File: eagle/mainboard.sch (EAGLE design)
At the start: 73 parts, among them IC1 74HC02D, IC2 74HC151D, IC3 74HC151D, IC4 74HC590D

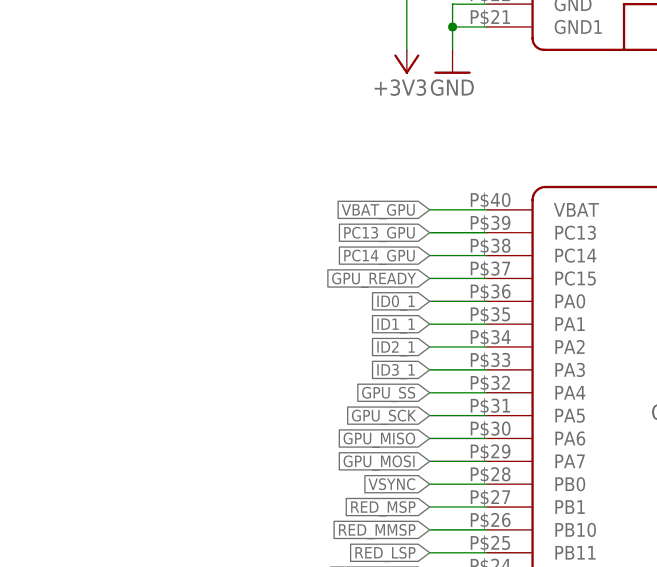
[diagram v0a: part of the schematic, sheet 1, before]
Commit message: pcb: gpu ready led
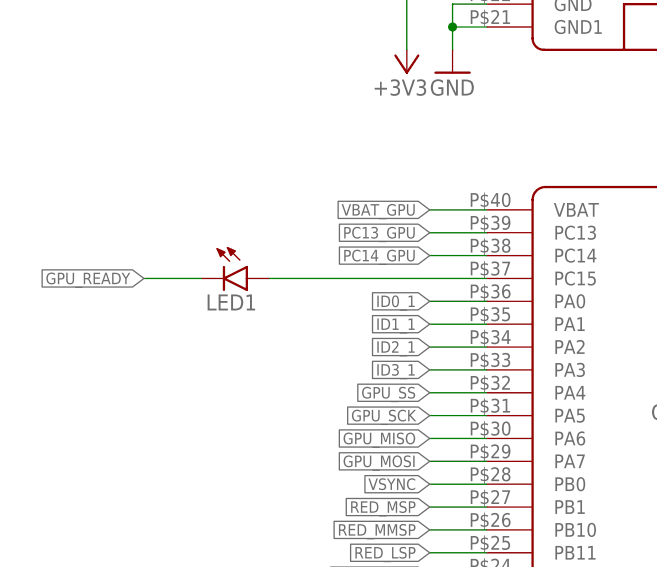
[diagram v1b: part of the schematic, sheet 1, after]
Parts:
- added LED1: (no value), led:LEDCHIPLED_0805
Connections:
- new net N$1: GPU.PC15, LED1.A
- net GPU_READY: now also LED1.C; no longer GPU.PC15
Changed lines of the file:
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@@
 <setting verticaltext="up"/>
 </settings>
-<grid distance="0.1" unitdist="inch" unit="inch" style="lines" multiple="1" display="no" altdistance="0.01" altunitdist="inch" altunit="inch"/>
+<grid distance="50" unitdist="mil" unit="mil" style="dots" multiple="1" display="yes" altdistance="0.01" altunitdist="inch" altunit="inch"/>
 <layers>
 <layer number="1" name="Top" color="4" fill="1" visible="no" active="no"/>
@@
 <part name="GND19" library="supply1" library_urn="urn:adsk.eagle:library:371" deviceset="GND" device=""/>
 <part name="GND22" library="supply1" library_urn="urn:adsk.eagle:library:371" deviceset="GND" device=""/>
+<part name="LED1" library="led" library_urn="urn:adsk.eagle:library:259" deviceset="LED" device="CHIPLED_0805" package3d_urn="urn:adsk.eagle:package:15821/2"/>
 </parts>
 <sheets>
@@
 <attribute name="VALUE" x="350.52" y="33.02" size="1.778" layer="96"/>
 </instance>
+<instance part="LED1" gate="G$1" x="77.47" y="92.71" smashed="yes" rot="R270">
+<attribute name="NAME" x="72.898" y="89.154" size="1.778" layer="95"/>
+<attribute name="VALUE" x="72.898" y="86.995" size="1.778" layer="96"/>
+</instance>
 </instances>
 <busses>
@@
 <net name="GPU_READY" class="0">
 <segment>
-<wire x1="97.79" y1="92.71" x2="104.14" y2="92.71" width="0.1524" layer="91"/>
-<label x="97.79" y="92.71" size="1.27" layer="95" rot="R180" xref="yes"/>
-<pinref part="GPU" gate="G$1" pin="PC15"/>
-</segment>
-<segment>
 <wire x1="97.79" y1="161.29" x2="104.14" y2="161.29" width="0.1524" layer="91"/>
 <label x="97.79" y="161.29" size="1.27" layer="95" rot="R180" xref="yes"/>
 <pinref part="CPU" gate="G$1" pin="PC15"/>
+</segment>
+<segment>
+<wire x1="66.04" y1="92.71" x2="72.39" y2="92.71" width="0.1524" layer="91"/>
+<label x="66.04" y="92.71" size="1.27" layer="95" rot="R180" xref="yes"/>
+<pinref part="LED1" gate="G$1" pin="C"/>
 </segment>
 </net>
@@
 </segment>
 </net>
+<net name="N$1" class="0">
+<segment>
+<pinref part="LED1" gate="G$1" pin="A"/>
+<pinref part="GPU" gate="G$1" pin="PC15"/>
+<wire x1="80.01" y1="92.71" x2="104.14" y2="92.71" width="0.1524" layer="91"/>
+</segment>
+</net>

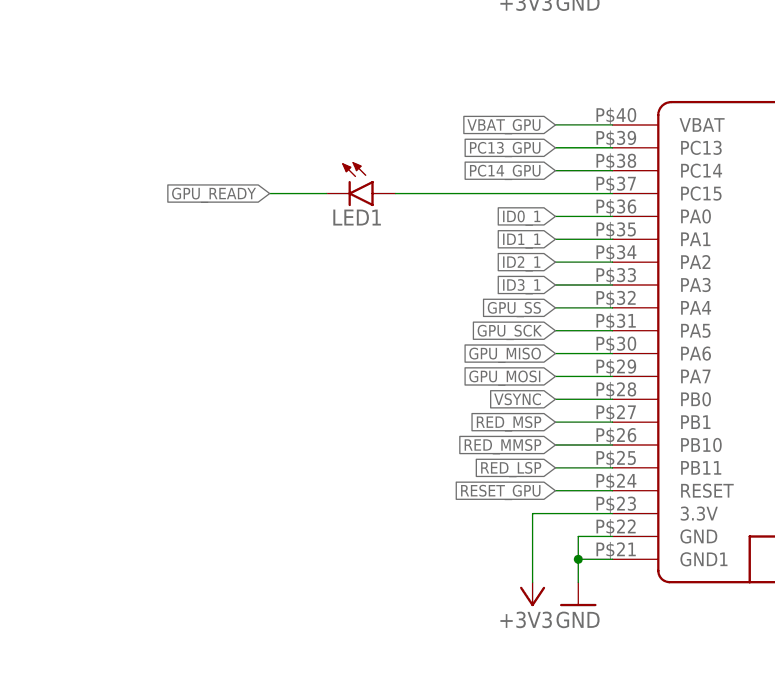
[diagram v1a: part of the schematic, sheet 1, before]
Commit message: made D-pad quadrtatic, corrected other minor stuff
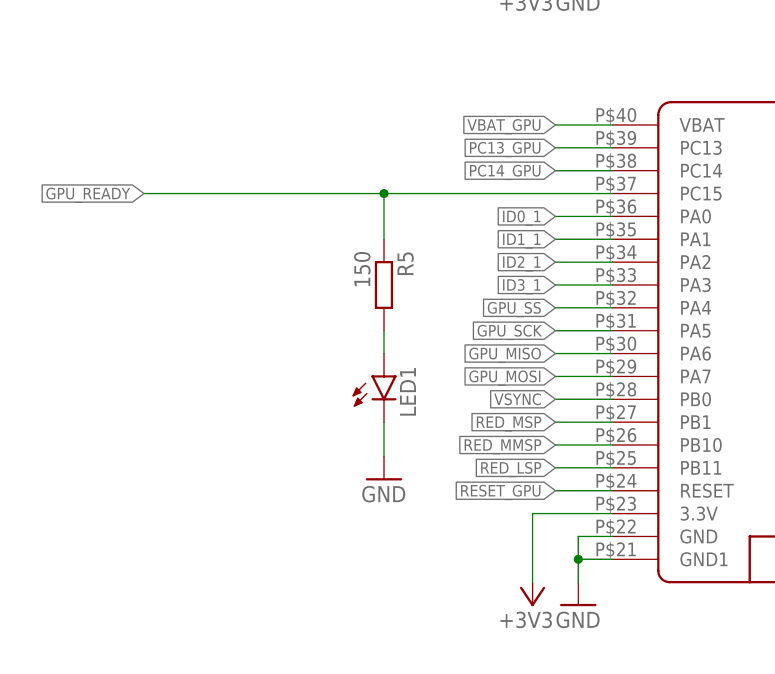
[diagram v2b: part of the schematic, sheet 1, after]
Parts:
- added R5: 150, rcl:R-EU_R0805
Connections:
- net GND: now also LED1.C
- net GPU_READY: now also GPU.PC15, R5.1; no longer LED1.C
- net N$1: now also R5.2; no longer GPU.PC15
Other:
- moved on the sheet: LED1
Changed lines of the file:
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@@
 <setting verticaltext="up"/>
 </settings>
-<grid distance="50" unitdist="mil" unit="mil" style="dots" multiple="1" display="yes" altdistance="0.01" altunitdist="inch" altunit="inch"/>
+<grid distance="0.1" unitdist="inch" unit="inch" style="lines" multiple="1" display="no" altdistance="0.01" altunitdist="inch" altunit="inch"/>
 <layers>
 <layer number="1" name="Top" color="4" fill="1" visible="no" active="no"/>
@@
 <part name="GND22" library="supply1" library_urn="urn:adsk.eagle:library:371" deviceset="GND" device=""/>
 <part name="LED1" library="led" library_urn="urn:adsk.eagle:library:259" deviceset="LED" device="CHIPLED_0805" package3d_urn="urn:adsk.eagle:package:15821/2"/>
+<part name="R5" library="rcl" library_urn="urn:adsk.eagle:library:334" deviceset="R-EU_" device="R0805" package3d_urn="urn:adsk.eagle:package:23553/2" value="150"/>
+<part name="GND32" library="supply1" library_urn="urn:adsk.eagle:library:371" deviceset="GND" device=""/>
 </parts>
 <sheets>
@@
 <attribute name="VALUE" x="350.52" y="33.02" size="1.778" layer="96"/>
 </instance>
-<instance part="LED1" gate="G$1" x="77.47" y="92.71" smashed="yes" rot="R270">
-<attribute name="NAME" x="72.898" y="89.154" size="1.778" layer="95"/>
-<attribute name="VALUE" x="72.898" y="86.995" size="1.778" layer="96"/>
+<instance part="LED1" gate="G$1" x="78.74" y="72.39" smashed="yes">
+<attribute name="NAME" x="82.296" y="67.818" size="1.778" layer="95" rot="R90"/>
+<attribute name="VALUE" x="84.455" y="67.818" size="1.778" layer="96" rot="R90"/>
+</instance>
+<instance part="R5" gate="G$1" x="78.74" y="82.55" smashed="yes" rot="R270">
+<attribute name="NAME" x="80.2386" y="86.36" size="1.778" layer="95" rot="R270"/>
+<attribute name="VALUE" x="75.438" y="86.36" size="1.778" layer="96" rot="R270"/>
+</instance>
+<instance part="GND32" gate="1" x="78.74" y="60.96" smashed="yes">
+<attribute name="VALUE" x="76.2" y="58.42" size="1.778" layer="96"/>
 </instance>
 </instances>
@@
 <pinref part="GND13" gate="1" pin="GND"/>
 </segment>
+<segment>
+<pinref part="LED1" gate="G$1" pin="C"/>
+<wire x1="78.74" y1="67.31" x2="78.74" y2="63.5" width="0.1524" layer="91"/>
+<pinref part="GND32" gate="1" pin="GND"/>
+</segment>
 </net>
 <net name="GPU_MOSI" class="0">
@@
 </segment>
 <segment>
-<wire x1="66.04" y1="92.71" x2="72.39" y2="92.71" width="0.1524" layer="91"/>
-<label x="66.04" y="92.71" size="1.27" layer="95" rot="R180" xref="yes"/>
-<pinref part="LED1" gate="G$1" pin="C"/>
+<label x="52.07" y="92.71" size="1.27" layer="95" rot="R180" xref="yes"/>
+<pinref part="R5" gate="G$1" pin="1"/>
+<wire x1="78.74" y1="92.71" x2="52.07" y2="92.71" width="0.1524" layer="91"/>
+<wire x1="78.74" y1="87.63" x2="78.74" y2="92.71" width="0.1524" layer="91"/>
+<pinref part="GPU" gate="G$1" pin="PC15"/>
+<wire x1="104.14" y1="92.71" x2="78.74" y2="92.71" width="0.1524" layer="91"/>
+<junction x="78.74" y="92.71"/>
 </segment>
 </net>
@@
 <net name="N$1" class="0">
 <segment>
+<pinref part="R5" gate="G$1" pin="2"/>
 <pinref part="LED1" gate="G$1" pin="A"/>
-<pinref part="GPU" gate="G$1" pin="PC15"/>
-<wire x1="80.01" y1="92.71" x2="104.14" y2="92.71" width="0.1524" layer="91"/>
-</segment>
-</net>
+<wire x1="78.74" y1="74.93" x2="78.74" y2="77.47" width="0.1524" layer="91"/>
+</segment>
+</net>

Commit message: added svg art and finished todo list
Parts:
- added JP5: (no value), pinhead:PINHD-1X2
- added LED2: (no value), led:LEDCHIPLED_0805
- added R26: 150, rcl:R-EU_R0805
- added R27: 10k, rcl:R-EU_R0805
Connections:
- new net N$2: LED2.A, R26.2
- net +5V: now also JP5.1
- net GND: now also R27.2
- net GNDA: now also LED2.C
- net PC14_GPU: now also JP5.2, R27.1
- net VCC: now also R26.1
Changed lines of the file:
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@@
 <setting verticaltext="up"/>
 </settings>
-<grid distance="0.1" unitdist="inch" unit="inch" style="lines" multiple="1" display="no" altdistance="0.01" altunitdist="inch" altunit="inch"/>
+<grid distance="50" unitdist="mil" unit="mil" style="lines" multiple="1" display="no" altdistance="0.01" altunitdist="inch" altunit="inch"/>
 <layers>
 <layer number="1" name="Top" color="4" fill="1" visible="no" active="no"/>
@@
 <part name="R5" library="rcl" library_urn="urn:adsk.eagle:library:334" deviceset="R-EU_" device="R0805" package3d_urn="urn:adsk.eagle:package:23553/2" value="150"/>
 <part name="GND32" library="supply1" library_urn="urn:adsk.eagle:library:371" deviceset="GND" device=""/>
+<part name="LED2" library="led" library_urn="urn:adsk.eagle:library:259" deviceset="LED" device="CHIPLED_0805" package3d_urn="urn:adsk.eagle:package:15821/2"/>
+<part name="R26" library="rcl" library_urn="urn:adsk.eagle:library:334" deviceset="R-EU_" device="R0805" package3d_urn="urn:adsk.eagle:package:23553/2" value="150"/>
+<part name="GND38" library="supply1" library_urn="urn:adsk.eagle:library:371" deviceset="GNDA" device=""/>
+<part name="JP5" library="pinhead" library_urn="urn:adsk.eagle:library:325" deviceset="PINHD-1X2" device="" package3d_urn="urn:adsk.eagle:package:22435/2"/>
+<part name="P+3" library="supply1" library_urn="urn:adsk.eagle:library:371" deviceset="+5V" device=""/>
+<part name="R27" library="rcl" library_urn="urn:adsk.eagle:library:334" deviceset="R-EU_" device="R0805" package3d_urn="urn:adsk.eagle:package:23553/2" value="10k"/>
+<part name="GND40" library="supply1" library_urn="urn:adsk.eagle:library:371" deviceset="GND" device=""/>
 </parts>
 <sheets>
@@
 <attribute name="VALUE" x="76.2" y="58.42" size="1.778" layer="96"/>
 </instance>
+<instance part="JP5" gate="G$1" x="82.55" y="100.33" smashed="yes">
+<attribute name="NAME" x="76.2" y="106.045" size="1.778" layer="95"/>
+<attribute name="VALUE" x="76.2" y="95.25" size="1.778" layer="96"/>
+</instance>
+<instance part="P+3" gate="1" x="78.74" y="111.76" smashed="yes">
+<attribute name="VALUE" x="82.55" y="114.3" size="1.778" layer="96" rot="R180"/>
+</instance>
+<instance part="R27" gate="G$1" x="71.12" y="82.55" smashed="yes" rot="R270">
+<attribute name="NAME" x="72.6186" y="86.36" size="1.778" layer="95" rot="R270"/>
+<attribute name="VALUE" x="67.818" y="86.36" size="1.778" layer="96" rot="R270"/>
+</instance>
+<instance part="GND40" gate="1" x="71.12" y="71.12" smashed="yes">
+<attribute name="VALUE" x="68.58" y="68.58" size="1.778" layer="96"/>
+</instance>
 </instances>
 <busses>
@@
 <wire x1="78.74" y1="67.31" x2="78.74" y2="63.5" width="0.1524" layer="91"/>
 <pinref part="GND32" gate="1" pin="GND"/>
+</segment>
+<segment>
+<pinref part="R27" gate="G$1" pin="2"/>
+<pinref part="GND40" gate="1" pin="GND"/>
+<wire x1="71.12" y1="77.47" x2="71.12" y2="73.66" width="0.1524" layer="91"/>
 </segment>
 </net>
@@
 <net name="PC14_GPU" class="0">
 <segment>
-<wire x1="97.79" y1="95.25" x2="104.14" y2="95.25" width="0.1524" layer="91"/>
-<label x="97.79" y="95.25" size="1.27" layer="95" rot="R180" xref="yes"/>
+<wire x1="67.31" y1="95.25" x2="71.12" y2="95.25" width="0.1524" layer="91"/>
+<label x="67.31" y="95.25" size="1.27" layer="95" rot="R180" xref="yes"/>
 <pinref part="GPU" gate="G$1" pin="PC14"/>
+<pinref part="JP5" gate="G$1" pin="2"/>
+<wire x1="71.12" y1="95.25" x2="78.74" y2="95.25" width="0.1524" layer="91"/>
+<wire x1="78.74" y1="95.25" x2="104.14" y2="95.25" width="0.1524" layer="91"/>
+<wire x1="80.01" y1="100.33" x2="78.74" y2="100.33" width="0.1524" layer="91"/>
+<wire x1="78.74" y1="100.33" x2="78.74" y2="95.25" width="0.1524" layer="91"/>
+<junction x="78.74" y="95.25"/>
+<pinref part="R27" gate="G$1" pin="1"/>
+<wire x1="71.12" y1="87.63" x2="71.12" y2="95.25" width="0.1524" layer="91"/>
+<junction x="71.12" y="95.25"/>
 </segment>
 </net>
@@
 <pinref part="P+2" gate="1" pin="+5V"/>
 <wire x1="157.48" y1="102.87" x2="157.48" y2="95.25" width="0.1524" layer="91"/>
+</segment>
+<segment>
+<pinref part="JP5" gate="G$1" pin="1"/>
+<wire x1="80.01" y1="102.87" x2="78.74" y2="102.87" width="0.1524" layer="91"/>
+<wire x1="78.74" y1="102.87" x2="78.74" y2="109.22" width="0.1524" layer="91"/>
+<pinref part="P+3" gate="1" pin="+5V"/>
 </segment>
 </net>
@@
 <attribute name="NAME" x="59.69" y="140.97" size="1.778" layer="95" align="center"/>
 <attribute name="VALUE" x="59.69" y="115.57" size="1.778" layer="96" align="center"/>
+</instance>
+<instance part="LED2" gate="G$1" x="22.86" y="115.57" smashed="yes">
+<attribute name="NAME" x="26.416" y="110.998" size="1.778" layer="95" rot="R90"/>
+<attribute name="VALUE" x="28.575" y="110.998" size="1.778" layer="96" rot="R90"/>
+</instance>
+<instance part="R26" gate="G$1" x="22.86" y="125.73" smashed="yes" rot="R270">
+<attribute name="NAME" x="24.3586" y="129.54" size="1.778" layer="95" rot="R270"/>
+<attribute name="VALUE" x="19.558" y="129.54" size="1.778" layer="96" rot="R270"/>
+</instance>
+<instance part="GND38" gate="1" x="22.86" y="104.14" smashed="yes" rot="MR0">
+<attribute name="VALUE" x="25.4" y="101.6" size="1.778" layer="96" rot="MR90"/>
 </instance>
 </instances>
@@
 <junction x="46.99" y="123.19"/>
 </segment>
+<segment>
+<pinref part="LED2" gate="G$1" pin="C"/>
+<wire x1="22.86" y1="110.49" x2="22.86" y2="106.68" width="0.1524" layer="91"/>
+<pinref part="GND38" gate="1" pin="GNDA"/>
+</segment>
 </net>
 <net name="VCC" class="0">
@@
 <pinref part="CONTROLLERIN" gate="G$1" pin="VCC"/>
 <wire x1="49.53" y1="135.89" x2="34.29" y2="135.89" width="0.1524" layer="91"/>
+<pinref part="R26" gate="G$1" pin="1"/>
+<wire x1="22.86" y1="130.81" x2="22.86" y2="135.89" width="0.1524" layer="91"/>
+<wire x1="22.86" y1="135.89" x2="34.29" y2="135.89" width="0.1524" layer="91"/>
 </segment>
 <segment>
@@
 </segment>
 </net>
+<net name="N$2" class="0">
+<segment>
+<pinref part="R26" gate="G$1" pin="2"/>
+<pinref part="LED2" gate="G$1" pin="A"/>
+<wire x1="22.86" y1="118.11" x2="22.86" y2="120.65" width="0.1524" layer="91"/>
+</segment>
+</net>

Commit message: pcb: v2 features
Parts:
- added JP6: (no value), pinhead:PINHD-1X2
- added LED3: (no value), led:LEDCHIPLED_0805
- added R28: 220, rcl:R-EU_R0805
- added R29: 10k, rcl:R-EU_R0805
- added S1: TL36PO, switch:TL36PO
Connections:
- removed net N$6: VGA.13
- removed net N$9: VGA.14
- removed net PB15_GPU: GPU.PB15
- new net N$3: POWERIN.VCC, S1.P
- new net N$4: LED3.A, R28.1
- new net PC14_GPU2: GPU.PB15, JP6.2, R29.1
- net +3V3: now also C1.1, C2.1, C3.1, C4.1, USBC1-2USBA.VBUS, USBC1-2USBB.VBUS, USB_C3-4USBA.VBUS, USB_C3-4USBB.VBUS
- net +5V: now also JP6.1, R28.2, S1.O; no longer C1.1, C2.1, C3.1, C4.1, POWERIN.VCC, USBC1-2USBA.VBUS, USBC1-2USBB.VBUS, USB_C3-4USBA.VBUS, USB_C3-4USBB.VBUS
- net GND: now also LED3.C, R29.2
- net HSYNC: now also VGA.13
- net VSYNC: now also VGA.14
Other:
- moved on the sheet: C5, JP5

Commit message: huber approved pcb 2.0
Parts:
- added R30, R31, R32, R33: 10k, rcl:R-EU_R0805
- S1: value TL36PO -> (none); device switch:TL36PO -> switches_SparkFun-Switches:SWITCH-SPDT-PTH-11.6X4.0MM
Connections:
- net +5V: now also S1.P; no longer S1.O
- net GND: now also R30.2, R31.2, R32.2, R33.2
- net GPU_MISO: now also R31.1
- net GPU_MOSI: now also R30.1
- net GPU_SCK: now also R32.1
- net GPU_SS: now also R33.1
- net N$3: now also S1.O; no longer S1.P
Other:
- moved on the sheet: JP5, LED1, R27, R5
